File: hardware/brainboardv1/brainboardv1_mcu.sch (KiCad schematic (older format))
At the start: 9 parts

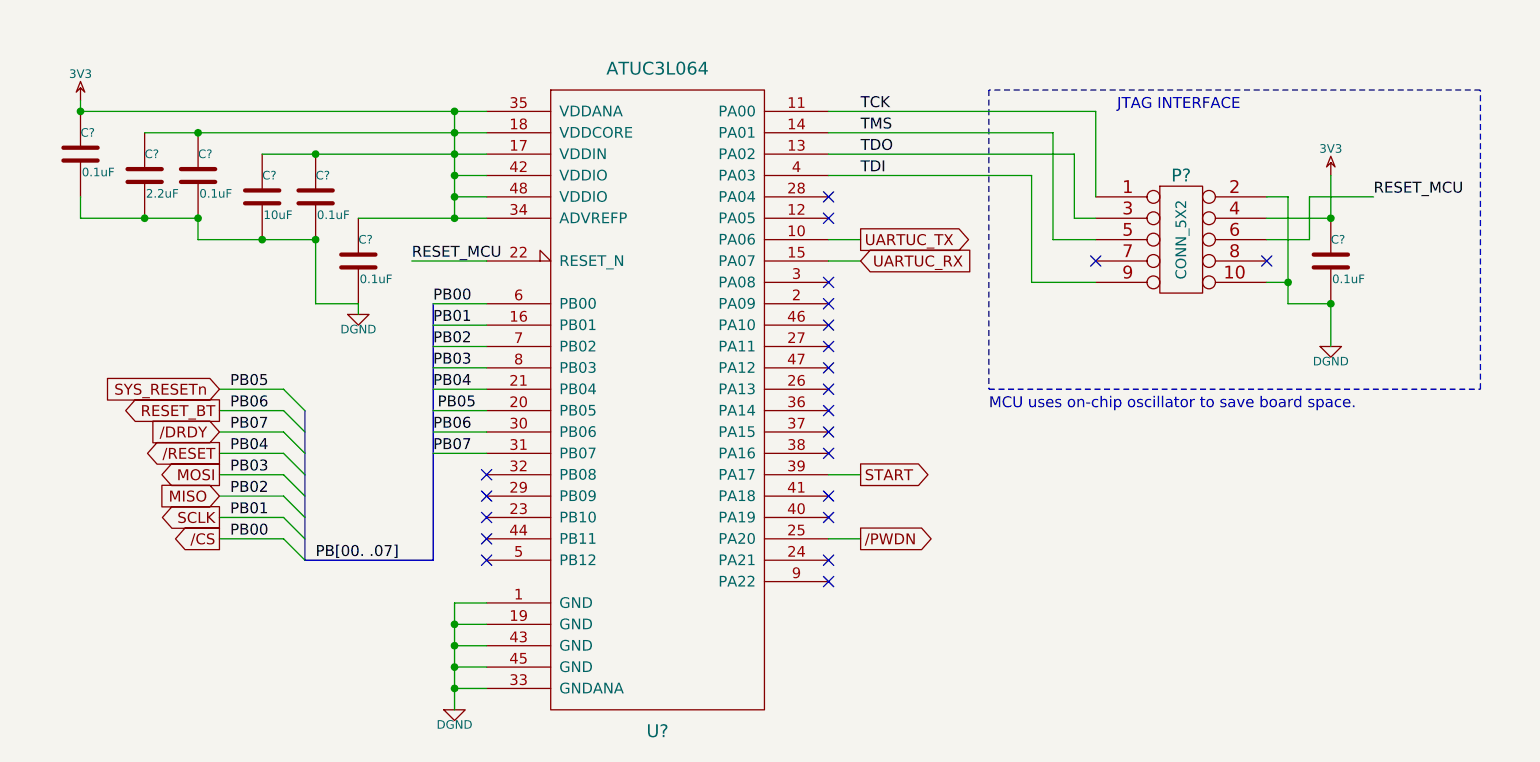
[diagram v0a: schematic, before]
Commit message: Nearly finished v1 sch & brd, await final check
Fixed errors from Rev 0, added MPU-6050 accelerometer/gyro for head
motion tracking, switched to +/-2.5V analog supply, added 2 bipolar
analog inputs for EOG tracking, added daisy-chain capability
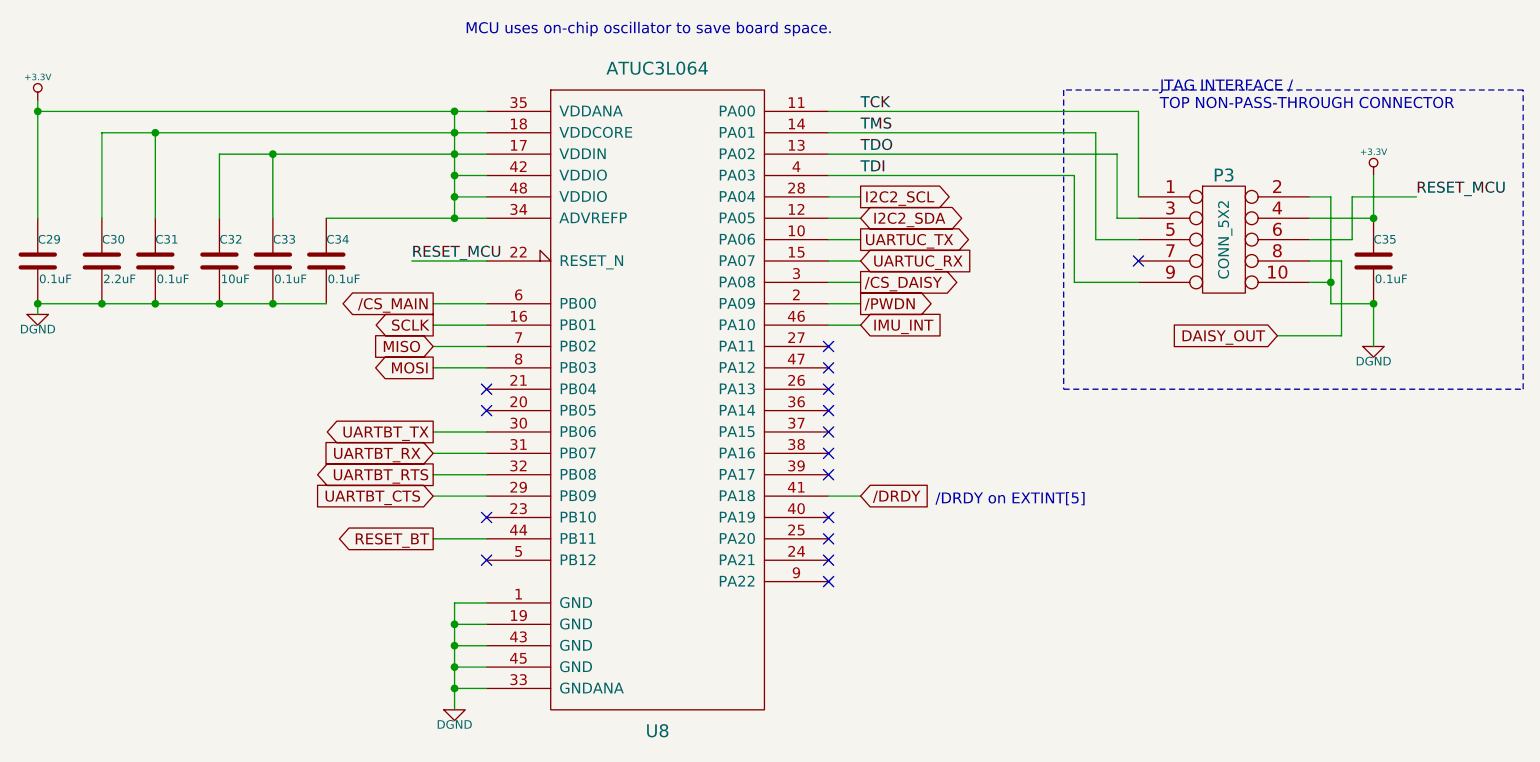
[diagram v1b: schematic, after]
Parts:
- removed C? (x5): 0.1uF, ~, symbol C
- removed C?: 10uF, ~, symbol C
- removed C?: 2.2uF, ~, symbol C
- removed P?: CONN_5X2, ~, symbol CONN_5X2
- removed U?: ATUC3L064, symbol ATUC3L064
- added C29, C31, C33, C34, C35: 0.1uF, ~, symbol C
- added C30: 2.2uF, ~, symbol C
- added C32: 10uF, ~, symbol C
- added P3: CONN_5X2, ~, symbol CONN_5X2
- added U8: ATUC3L064, symbol ATUC3L064
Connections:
- net /DRDY: now also U8.41 (PA18)
- net /PWDN: now also U8.2 (PA09)
- net DGND: now also C29.2, C30.2, C31.2, C32.2, C33.2, C34.2, C35.2, P3.10, P3.2, U8.1 (GND), U8.19 (GND), U8.33 (GNDANA), U8.43 (GND), U8.45 (GND)
- net MISO: now also U8.7 (PB02)
- net MOSI: now also U8.8 (PB03)
- net RESET_BT: now also U8.44 (PB11)
- net RESET_MCU: now also P3.6, U8.22 (RESET_N)
- net SCLK: now also U8.16 (PB01)
- net TCK: now also P3.1, U8.11 (PA00)
- net TDI: now also P3.9, U8.4 (PA03)
- net TDO: now also P3.3, U8.13 (PA02)
- net TMS: now also P3.5, U8.14 (PA01)
- net UARTUC_RX: now also U8.15 (PA07)
- net UARTUC_TX: now also U8.10 (PA06)
- new net +3.3V: C29.1, C30.1, C31.1, C32.1, C33.1, C34.1, C35.1, P3.4, U8.17 (VDDIN), U8.18 (VDDCORE), U8.34 (ADVREFP), U8.35 (VDDANA), U8.42 (VDDIO), U8.48 (VDDIO)
- new net /CS_DAISY: U8.3 (PA08)
- new net /CS_MAIN: U8.6 (PB00)
- new net DAISY_OUT: P3.8
- new net I2C2_SCL: U8.28 (PA04)
- new net I2C2_SDA: U8.12 (PA05)
- new net IMU_INT: U8.46 (PA10)
- new net UARTBT_CTS: U8.29 (PB09)
- new net UARTBT_RTS: U8.32 (PB08)
- new net UARTBT_RX: U8.31 (PB07)
- new net UARTBT_TX: U8.30 (PB06)
- no-connect marks 22 -> 16
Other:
- note added: "/DRDY on EXTINT[5]"
- note added: "JTAG INTERFACE /\nTOP NON-PASS-THROUGH CONNECTOR"
- note removed: "JTAG INTERFACE"
